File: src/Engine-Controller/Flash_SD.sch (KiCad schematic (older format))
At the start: 2 parts

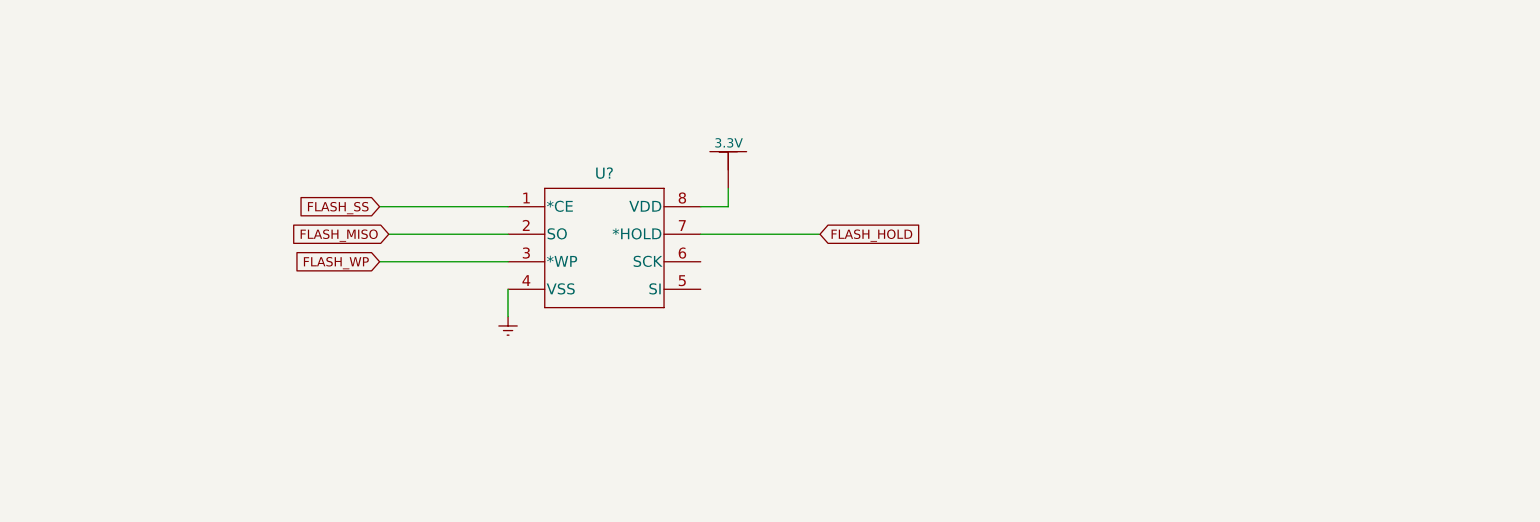
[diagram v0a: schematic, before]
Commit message: Added Micro SD Card
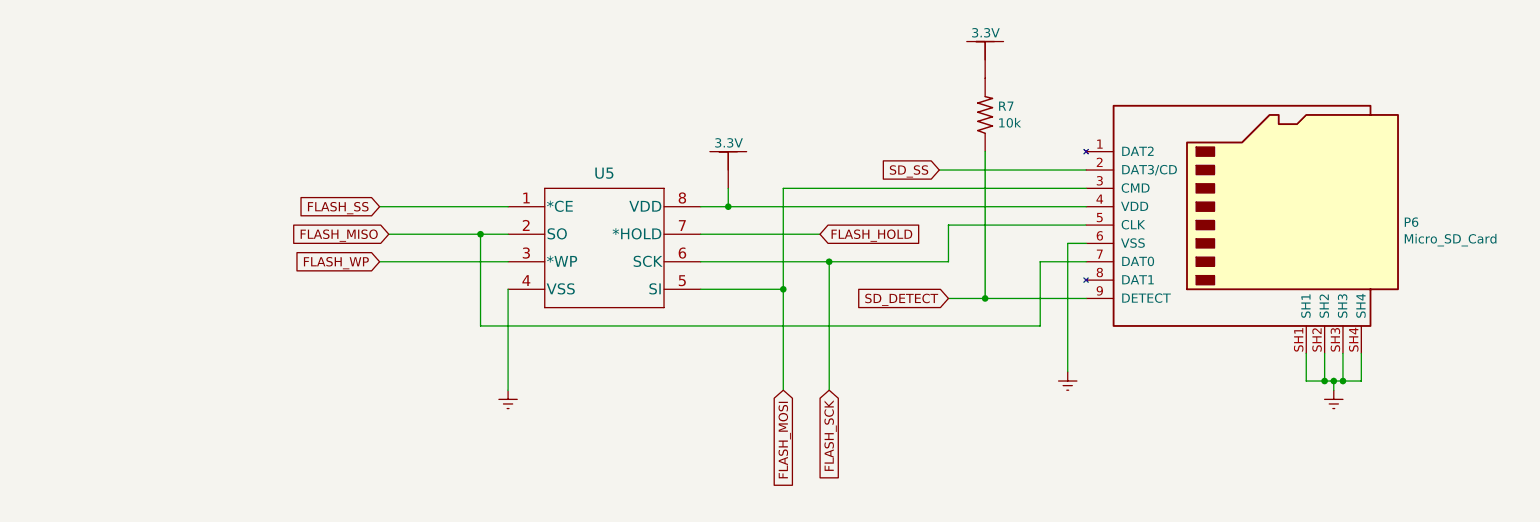
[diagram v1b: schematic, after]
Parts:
- added None06: 3.3V, symbol Engine-Controller:3.3V
- added P6: Micro_SD_Card, symbol Engine-Controller:Micro_SD_Card
- added R7: 10k, symbol Engine-Controller:RES_0603
- gave numbers to parts that had none: 2
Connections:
- net Earth: now also P6.6 (VSS), P6.SH1, P6.SH2, P6.SH3, P6.SH4
- net FLASH_MISO: now also P6.7 (DAT0)
- net FLASH_MOSI: now reaches U5.5 (SI)
- net FLASH_MOSI: now also P6.3 (CMD)
- net FLASH_SCK: now reaches U5.6 (SCK)
- net FLASH_SCK: now also P6.5 (CLK)
- net at None05.~, U5.8 (VDD): now also P6.4 (VDD)
- new net: None06.~, R7.2
- new net SD_DETECT: P6.9 (DETECT), R7.1
- new net SD_SS: P6.2 (DAT3/CD)
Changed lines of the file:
@@
 $EndDescr
 $Comp
-L Engine-Controller:SST25VF040B-50-4I-S2AE-T U?
+L Engine-Controller:SST25VF040B-50-4I-S2AE-T U5
 U 1 1 617854EA
 P 5950 3950
-F 0 "U?" H 5925 4231 60  0000 C CNN
+F 0 "U5" H 5925 4231 60  0000 C CNN
 F 1 "SST25VF040B-50-4I-S2AE-T" H 5925 4231 60  0001 C CNN
 F 2 "SOIC8_S2A_SST_MCH" H 5950 3250 60  0001 C CNN
@@
 FLASH_MISO
 Wire Wire Line
-	5400 4000 4750 4000
+	5400 4000 5250 4000
 Text GLabel 4700 4150 0    50   Input ~ 0
 FLASH_WP
@@
 	5400 4150 4700 4150
 $Comp
-L Engine-Controller:3.3V None?
+L Engine-Controller:3.3V None05
 U 1 1 617870C5
 P 6600 3600
-F 0 "None?" H 6728 3589 50  0001 L CNN
+F 0 "None05" H 6728 3589 50  0001 L CNN
 F 1 "3.3V" H 6524 3696 50  0000 L CNN
 F 2 "" H 6600 3600 50  0001 C CNN
@@
 	6600 3850 6600 3750
 $Comp
-L power:Earth #PWR?
+L power:Earth #PWR03
 U 1 1 61788B6E
-P 5400 4450
-F 0 "#PWR?" H 5400 4200 50  0001 C CNN
-F 1 "Earth" H 5400 4300 50  0001 C CNN
-F 2 "" H 5400 4450 50  0001 C CNN
-F 3 "~" H 5400 4450 50  0001 C CNN
-	1    5400 4450
+P 5400 4850
+F 0 "#PWR03" H 5400 4600 50  0001 C CNN
+F 1 "Earth" H 5400 4700 50  0001 C CNN
+F 2 "" H 5400 4850 50  0001 C CNN
+F 3 "~" H 5400 4850 50  0001 C CNN
+	1    5400 4850
 	1    0    0    -1
 $EndComp
-Wire Wire Line
-	5400 4300 5400 4450
 Text GLabel 7100 4000 2    50   Input ~ 0
 FLASH_HOLD
 Wire Wire Line
 	6450 4000 7100 4000
+Text GLabel 7150 4850 3    50   Input ~ 0
+FLASH_SCK
+Wire Wire Line
+	7150 4150 6450 4150
+Text GLabel 6900 4850 3    50   Input ~ 0
+FLASH_MOSI
+$Comp
+L Engine-Controller:Micro_SD_Card P6
+U 1 1 617F7CCB
+P 9450 3850
+F 0 "P6" H 10280 3764 50  0000 L CNN
+F 1 "Micro_SD_Card" H 10280 3673 50  0000 L CNN
+F 2 "" H 10600 4150 50  0001 C CNN
+F 3 "http://katalog.we-online.de/em/datasheet/693072010801.pdf" H 9450 3850 50  0001 C CNN
+	1    9450 3850
+	1    0    0    -1
+$EndComp
+$Comp
+L power:Earth #PWR05
+U 1 1 617F979C
+P 9900 4850
+F 0 "#PWR05" H 9900 4600 50  0001 C CNN
+F 1 "Earth" H 9900 4700 50  0001 C CNN
+F 2 "" H 9900 4850 50  0001 C CNN
+F 3 "~" H 9900 4850 50  0001 C CNN
+	1    9900 4850
+	1    0    0    -1
+$EndComp
+Wire Wire Line
+	9750 4650 9750 4800
+Wire Wire Line
+	9750 4800 9850 4800
+Wire Wire Line
+	9900 4800 9900 4850
+Wire Wire Line
+	9850 4650 9850 4800
+Connection ~ 9850 4800
+Wire Wire Line
+	9850 4800 9900 4800
+Wire Wire Line
+	9950 4650 9950 4800
+Wire Wire Line
+	9950 4800 9900 4800
+Connection ~ 9900 4800
+Wire Wire Line
+	10050 4650 10050 4800
+Wire Wire Line
+	10050 4800 9950 4800
+Connection ~ 9950 4800
+Wire Wire Line
+	6600 3850 8550 3850
+Connection ~ 6600 3850
+Text GLabel 7750 3650 0    50   Input ~ 0
+SD_SS
+Wire Wire Line
+	8550 3650 7750 3650
+Wire Wire Line
+	6900 4300 6900 3750
+Wire Wire Line
+	6900 3750 8550 3750
+Connection ~ 6900 4300
+Wire Wire Line
+	6900 4300 6450 4300
+Wire Wire Line
+	7150 4150 7800 4150
+Wire Wire Line
+	7800 4150 7800 3950
+Wire Wire Line
+	7800 3950 8550 3950
+Connection ~ 7150 4150
+$Comp
+L power:Earth #PWR04
+U 1 1 6180735A
+P 8450 4750
+F 0 "#PWR04" H 8450 4500 50  0001 C CNN
+F 1 "Earth" H 8450 4600 50  0001 C CNN
+F 2 "" H 8450 4750 50  0001 C CNN
+F 3 "~" H 8450 4750 50  0001 C CNN
+	1    8450 4750
+	1    0    0    -1
+$EndComp
+Wire Wire Line
+	8550 4050 8450 4050
+Wire Wire Line
+	8450 4050 8450 4750
+Wire Wire Line
+	6900 4300 6900 4850
+Wire Wire Line
+	7150 4150 7150 4850
+Wire Wire Line
+	5400 4300 5400 4850
+Wire Wire Line
+	5250 4000 5250 4500
+Wire Wire Line
+	5250 4500 8300 4500
+Wire Wire Line
+	8300 4500 8300 4150
+Wire Wire Line
+	8300 4150 8550 4150
+Connection ~ 5250 4000
+Wire Wire Line
+	5250 4000 4750 4000
+Text GLabel 7800 4350 0    50   Input ~ 0
+SD_DETECT
+Wire Wire Line
+	8550 4350 8000 4350
+$Comp
+L Engine-Controller:RES_0603 R7
+U 1 1 618D69C9
+P 8000 3350
+F 0 "R7" V 8046 3281 50  0000 R CNN
+F 1 "10k" V 7955 3281 50  0000 R CNN
+F 2 "" H 8050 2850 50  0001 L BNN
+F 3 "" H 8000 3350 50  0001 L BNN
+	1    8000 3350
+	0    -1   -1   0
+$EndComp
+Wire Wire Line
+	8000 3550 8000 4350
+Connection ~ 8000 4350
+Wire Wire Line
+	8000 4350 7800 4350
+$Comp
+L Engine-Controller:3.3V None06
+U 1 1 618DC655
+P 8000 3000
+F 0 "None06" H 8128 2989 50  0001 L CNN
+F 1 "3.3V" H 7924 3096 50  0000 L CNN
+F 2 "" H 8000 3000 50  0001 C CNN
+F 3 "" H 8000 3000 50  0001 C CNN
+	1    8000 3000
+	1    0    0    -1
+$EndComp
 $EndSCHEMATC

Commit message: Grounded USB shield
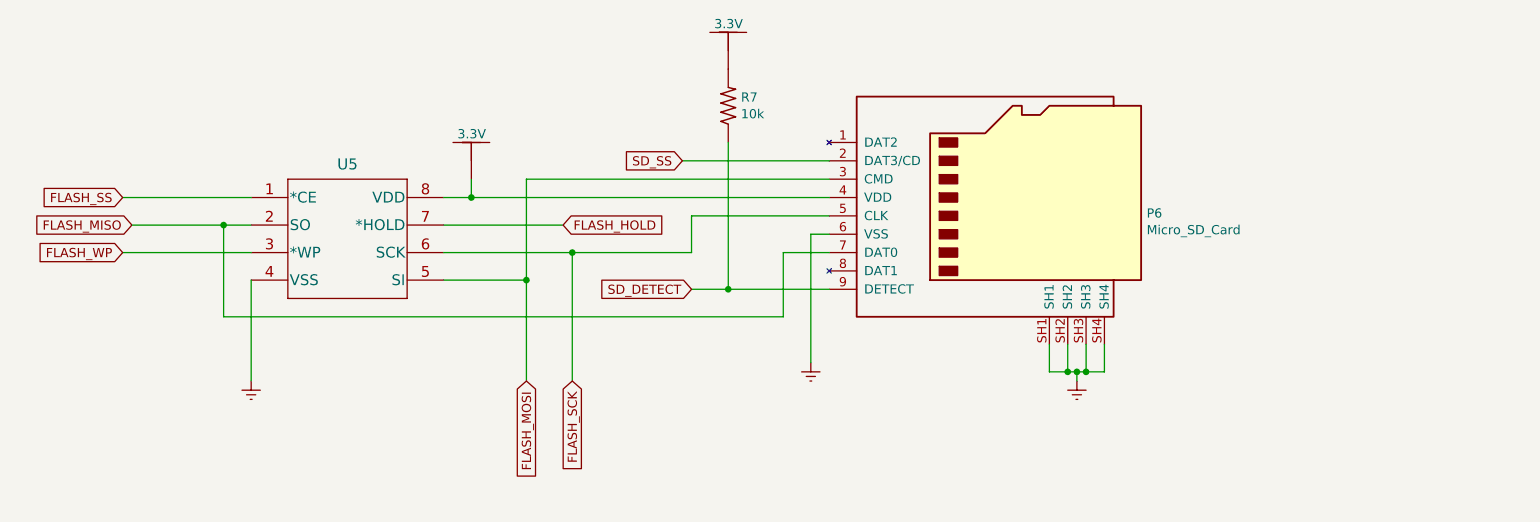
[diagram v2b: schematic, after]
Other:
- moved on the sheet: P6, R7, U5
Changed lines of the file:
@@
 L Engine-Controller:SST25VF040B-50-4I-S2AE-T U5
 U 1 1 617854EA
-P 5950 3950
-F 0 "U5" H 5925 4231 60  0000 C CNN
-F 1 "SST25VF040B-50-4I-S2AE-T" H 5925 4231 60  0001 C CNN
-F 2 "SOIC8_S2A_SST_MCH" H 5950 3250 60  0001 C CNN
-F 3 "" H 4750 4000 60  0001 C CNN
-	1    5950 3950
+P 4550 3900
+F 0 "U5" H 4525 4181 60  0000 C CNN
+F 1 "SST25VF040B-50-4I-S2AE-T" H 4525 4181 60  0001 C CNN
+F 2 "SOIC8_S2A_SST_MCH" H 4550 3200 60  0001 C CNN
+F 3 "" H 3350 3950 60  0001 C CNN
+	1    4550 3900
 	1    0    0    -1
 $EndComp
-Text GLabel 4700 3850 0    50   Input ~ 0
+Text GLabel 3300 3800 0    50   Input ~ 0
 FLASH_SS
 Wire Wire Line
-	4700 3850 5400 3850
-Text GLabel 4750 4000 0    50   Input ~ 0
+	3300 3800 4000 3800
+Text GLabel 3350 3950 0    50   Input ~ 0
 FLASH_MISO
 Wire Wire Line
-	5400 4000 5250 4000
-Text GLabel 4700 4150 0    50   Input ~ 0
+	4000 3950 3850 3950
+Text GLabel 3300 4100 0    50   Input ~ 0
 FLASH_WP
 Wire Wire Line
-	5400 4150 4700 4150
+	4000 4100 3300 4100
 $Comp
 L Engine-Controller:3.3V None05
 U 1 1 617870C5
-P 6600 3600
-F 0 "None05" H 6728 3589 50  0001 L CNN
-F 1 "3.3V" H 6524 3696 50  0000 L CNN
-F 2 "" H 6600 3600 50  0001 C CNN
-F 3 "" H 6600 3600 50  0001 C CNN
-	1    6600 3600
+P 5200 3550
+F 0 "None05" H 5328 3539 50  0001 L CNN
+F 1 "3.3V" H 5124 3646 50  0000 L CNN
+F 2 "" H 5200 3550 50  0001 C CNN
+F 3 "" H 5200 3550 50  0001 C CNN
+	1    5200 3550
 	1    0    0    -1
 $EndComp
 Wire Wire Line
-	6450 3850 6600 3850
+	5050 3800 5200 3800
 Wire Wire Line
-	6600 3850 6600 3750
+	5200 3800 5200 3700
 $Comp
 L power:Earth #PWR03
 U 1 1 61788B6E
-P 5400 4850
-F 0 "#PWR03" H 5400 4600 50  0001 C CNN
-F 1 "Earth" H 5400 4700 50  0001 C CNN
-F 2 "" H 5400 4850 50  0001 C CNN
-F 3 "~" H 5400 4850 50  0001 C CNN
-	1    5400 4850
+P 4000 4800
+F 0 "#PWR03" H 4000 4550 50  0001 C CNN
+F 1 "Earth" H 4000 4650 50  0001 C CNN
+F 2 "" H 4000 4800 50  0001 C CNN
+F 3 "~" H 4000 4800 50  0001 C CNN
+	1    4000 4800
 	1    0    0    -1
 $EndComp
-Text GLabel 7100 4000 2    50   Input ~ 0
+Text GLabel 5700 3950 2    50   Input ~ 0
 FLASH_HOLD
 Wire Wire Line
-	6450 4000 7100 4000
-Text GLabel 7150 4850 3    50   Input ~ 0
+	5050 3950 5700 3950
+Text GLabel 5750 4800 3    50   Input ~ 0
 FLASH_SCK
 Wire Wire Line
-	7150 4150 6450 4150
-Text GLabel 6900 4850 3    50   Input ~ 0
+	5750 4100 5050 4100
+Text GLabel 5500 4800 3    50   Input ~ 0
 FLASH_MOSI
 $Comp
 L Engine-Controller:Micro_SD_Card P6
 U 1 1 617F7CCB
-P 9450 3850
-F 0 "P6" H 10280 3764 50  0000 L CNN
-F 1 "Micro_SD_Card" H 10280 3673 50  0000 L CNN
-F 2 "" H 10600 4150 50  0001 C CNN
-F 3 "http://katalog.we-online.de/em/datasheet/693072010801.pdf" H 9450 3850 50  0001 C CNN
-	1    9450 3850
+P 8050 3800
+F 0 "P6" H 8880 3714 50  0000 L CNN
+F 1 "Micro_SD_Card" H 8880 3623 50  0000 L CNN
+F 2 "" H 9200 4100 50  0001 C CNN
+F 3 "http://katalog.we-online.de/em/datasheet/693072010801.pdf" H 8050 3800 50  0001 C CNN
+	1    8050 3800
 	1    0    0    -1
 $EndComp
@@
 L power:Earth #PWR05
 U 1 1 617F979C
-P 9900 4850
-F 0 "#PWR05" H 9900 4600 50  0001 C CNN
-F 1 "Earth" H 9900 4700 50  0001 C CNN
-F 2 "" H 9900 4850 50  0001 C CNN
-F 3 "~" H 9900 4850 50  0001 C CNN
-	1    9900 4850
+P 8500 4800
+F 0 "#PWR05" H 8500 4550 50  0001 C CNN
+F 1 "Earth" H 8500 4650 50  0001 C CNN
+F 2 "" H 8500 4800 50  0001 C CNN
+F 3 "~" H 8500 4800 50  0001 C CNN
+	1    8500 4800
 	1    0    0    -1
 $EndComp
 Wire Wire Line
-	9750 4650 9750 4800
+	8350 4600 8350 4750
 Wire Wire Line
-	9750 4800 9850 4800
+	8350 4750 8450 4750
 Wire Wire Line
-	9900 4800 9900 4850
+	8500 4750 8500 4800
 Wire Wire Line
-	9850 4650 9850 4800
-Connection ~ 9850 4800
+	8450 4600 8450 4750
+Connection ~ 8450 4750
 Wire Wire Line
-	9850 4800 9900 4800
+	8450 4750 8500 4750
 Wire Wire Line
-	9950 4650 9950 4800
+	8550 4600 8550 4750
 Wire Wire Line
-	9950 4800 9900 4800
-Connection ~ 9900 4800
+	8550 4750 8500 4750
+Connection ~ 8500 4750
 Wire Wire Line
-	10050 4650 10050 4800
+	8650 4600 8650 4750
 Wire Wire Line
-	10050 4800 9950 4800
-Connection ~ 9950 4800
+	8650 4750 8550 4750
+Connection ~ 8550 4750
 Wire Wire Line
-	6600 3850 8550 3850
-Connection ~ 6600 3850
-Text GLabel 7750 3650 0    50   Input ~ 0
+	5200 3800 7150 3800
+Connection ~ 5200 3800
+Text GLabel 6350 3600 0    50   Input ~ 0
 SD_SS
 Wire Wire Line
-	8550 3650 7750 3650
+	7150 3600 6350 3600
 Wire Wire Line
-	6900 4300 6900 3750
+	5500 4250 5500 3700
 Wire Wire Line
-	6900 3750 8550 3750
-Connection ~ 6900 4300
+	5500 3700 7150 3700
+Connection ~ 5500 4250
 Wire Wire Line
-	6900 4300 6450 4300
+	5500 4250 5050 4250
 Wire Wire Line
-	7150 4150 7800 4150
+	5750 4100 6400 4100
 Wire Wire Line
-	7800 4150 7800 3950
+	6400 4100 6400 3900
 Wire Wire Line
-	7800 3950 8550 3950
-Connection ~ 7150 4150
+	6400 3900 7150 3900
+Connection ~ 5750 4100
 $Comp
 L power:Earth #PWR04
 U 1 1 6180735A
-P 8450 4750
-F 0 "#PWR04" H 8450 4500 50  0001 C CNN
-F 1 "Earth" H 8450 4600 50  0001 C CNN
-F 2 "" H 8450 4750 50  0001 C CNN
-F 3 "~" H 8450 4750 50  0001 C CNN
-	1    8450 4750
+P 7050 4700
+F 0 "#PWR04" H 7050 4450 50  0001 C CNN
+F 1 "Earth" H 7050 4550 50  0001 C CNN
+F 2 "" H 7050 4700 50  0001 C CNN
+F 3 "~" H 7050 4700 50  0001 C CNN
+	1    7050 4700
 	1    0    0    -1
 $EndComp
 Wire Wire Line
-	8550 4050 8450 4050
+	7150 4000 7050 4000
 Wire Wire Line
-	8450 4050 8450 4750
+	7050 4000 7050 4700
 Wire Wire Line
-	6900 4300 6900 4850
+	5500 4250 5500 4800
 Wire Wire Line
-	7150 4150 7150 4850
+	5750 4100 5750 4800
 Wire Wire Line
-	5400 4300 5400 4850
+	4000 4250 4000 4800
 Wire Wire Line
-	5250 4000 5250 4500
+	3850 3950 3850 4450
 Wire Wire Line
-	5250 4500 8300 4500
+	3850 4450 6900 4450
 Wire Wire Line
-	8300 4500 8300 4150
+	6900 4450 6900 4100
 Wire Wire Line
-	8300 4150 8550 4150
-Connection ~ 5250 4000
+	6900 4100 7150 4100
+Connection ~ 3850 3950
 Wire Wire Line
-	5250 4000 4750 4000
-Text GLabel 7800 4350 0    50   Input ~ 0
+	3850 3950 3350 3950
+Text GLabel 6400 4300 0    50   Input ~ 0
 SD_DETECT
 Wire Wire Line
-	8550 4350 8000 4350
+	7150 4300 6600 4300
 $Comp
 L Engine-Controller:RES_0603 R7
 U 1 1 618D69C9
-P 8000 3350
-F 0 "R7" V 8046 3281 50  0000 R CNN
-F 1 "10k" V 7955 3281 50  0000 R CNN
-F 2 "" H 8050 2850 50  0001 L BNN
-F 3 "" H 8000 3350 50  0001 L BNN
-	1    8000 3350
+P 6600 3300
+F 0 "R7" V 6646 3231 50  0000 R CNN
+F 1 "10k" V 6555 3231 50  0000 R CNN
+F 2 "" H 6650 2800 50  0001 L BNN
+F 3 "" H 6600 3300 50  0001 L BNN
+	1    6600 3300
 	0    -1   -1   0
 $EndComp
 Wire Wire Line
-	8000 3550 8000 4350
-Connection ~ 8000 4350
+	6600 3500 6600 4300
+Connection ~ 6600 4300
 Wire Wire Line
-	8000 4350 7800 4350
+	6600 4300 6400 4300
 $Comp
 L Engine-Controller:3.3V None06
 U 1 1 618DC655
-P 8000 3000
-F 0 "None06" H 8128 2989 50  0001 L CNN
-F 1 "3.3V" H 7924 3096 50  0000 L CNN
-F 2 "" H 8000 3000 50  0001 C CNN
-F 3 "" H 8000 3000 50  0001 C CNN
-	1    8000 3000
+P 6600 2950
+F 0 "None06" H 6728 2939 50  0001 L CNN
+F 1 "3.3V" H 6524 3046 50  0000 L CNN
+F 2 "" H 6600 2950 50  0001 C CNN
+F 3 "" H 6600 2950 50  0001 C CNN
+	1    6600 2950
 	1    0    0    -1
 $EndComp
